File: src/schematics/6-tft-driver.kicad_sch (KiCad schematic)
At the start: 0 parts

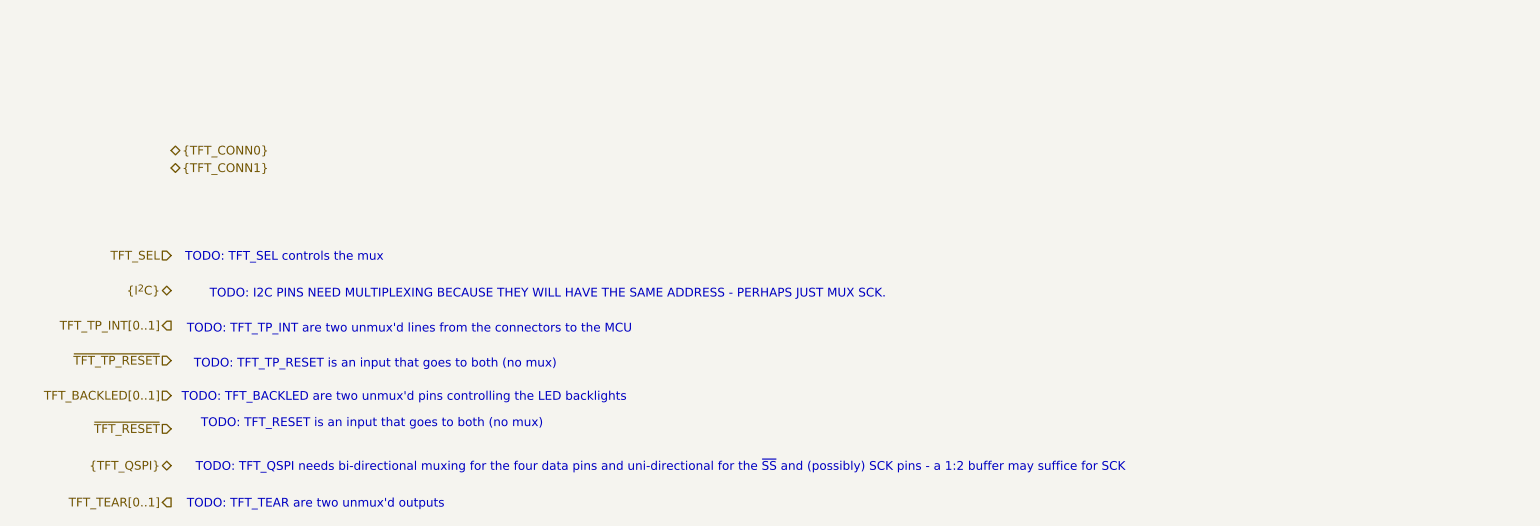
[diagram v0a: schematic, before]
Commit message: Further MCU elaboration and pin mapping.
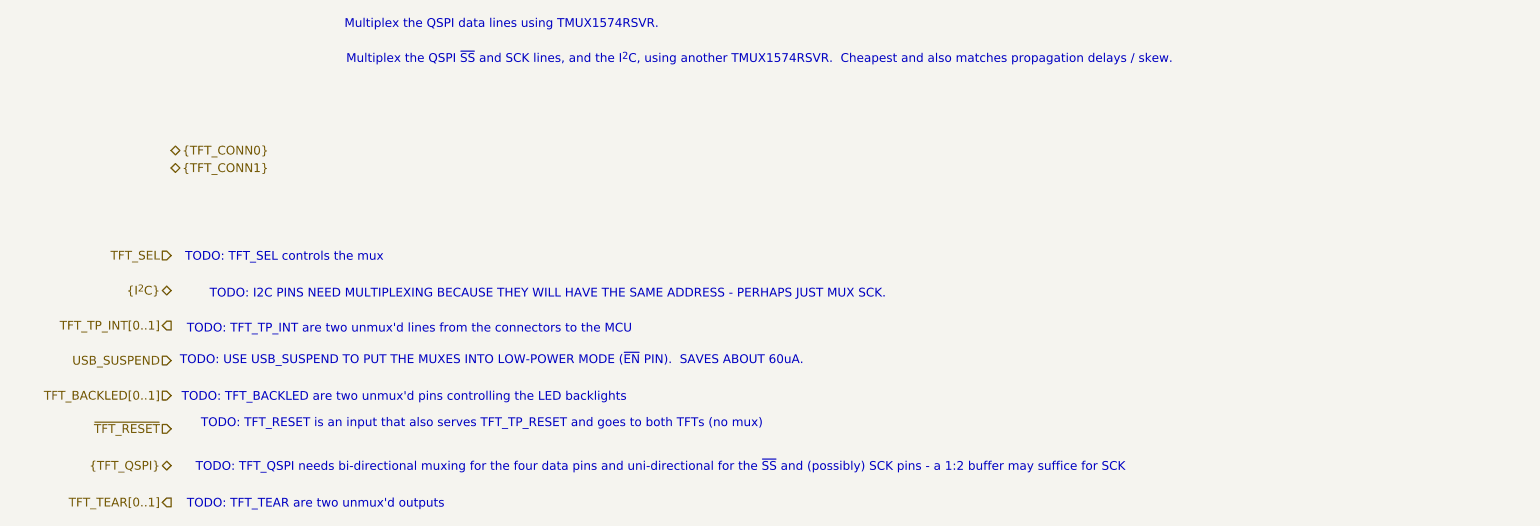
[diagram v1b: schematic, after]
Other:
- note added: "Multiplex the QSPI data lines using TMUX1574RSVR."
- note added: "Multiplex the QSPI ~{SS} and SCK lines, and the I^{2}C, using another TMUX1574RSVR. Cheapest and also matches propagation delays / skew."
- note added: "TODO: TFT_RESET is an input that also serves TFT_TP_RESET and goes to both TFTs (no mux)"
- note added: "TODO: USE USB_SUSPEND TO PUT THE MUXES INTO LOW-POWER MODE (~{EN} PIN). SAVES ABOUT 60uA."
- note removed: "TODO: TFT_RESET is an input that goes to both (no mux)"
- note removed: "TODO: TFT_TP_RESET is an input that goes to both (no mux)"
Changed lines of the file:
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@@
   (bus_alias "TFT_CONN0" (members "TP_SCL" "TP_SDA" "TP_INT" "TP_RST" "LEDA" "LEDK" "L_RES" "L_SDIN" "L_SCLK" "L_IO[1..3]" "L_CS" "L_TE"))
   (bus_alias "TFT_QSPI" (members "~{SS}" "SCK" "DATA[0..3]"))
+  (text "Multiplex the QSPI data lines using TMUX1574RSVR." (at 152.146 119.634 0)
+    (effects (font (size 1.27 1.27)) (justify left bottom))
+  )
   (text "TODO: TFT_QSPI needs bi-directional muxing for the four data pins and uni-directional for the ~{SS} and (possibly) SCK pins - a 1:2 buffer may suffice for SCK"
     (at 130.556 183.896 0)
@@
   (text "TODO: TFT_BACKLED are two unmux'd pins controlling the LED backlights"
     (at 128.524 173.736 0)
-    (effects (font (size 1.27 1.27)) (justify left bottom))
-  )
-  (text "TODO: TFT_TP_RESET is an input that goes to both (no mux)"
-    (at 130.302 168.91 0)
     (effects (font (size 1.27 1.27)) (justify left bottom))
   )
@@
     (effects (font (size 1.27 1.27)) (justify left bottom))
   )
+  (text "TODO: USE USB_SUSPEND TO PUT THE MUXES INTO LOW-POWER MODE (~{EN} PIN).  SAVES ABOUT 60uA."
+    (at 128.27 168.402 0)
+    (effects (font (size 1.27 1.27)) (justify left bottom))
+  )
   (text "TODO: TFT_TP_INT are two unmux'd lines from the connectors to the MCU"
     (at 129.286 163.83 0)
     (effects (font (size 1.27 1.27)) (justify left bottom))
   )
-  (text "TODO: TFT_RESET is an input that goes to both (no mux)"
+  (text "Multiplex the QSPI ~{SS} and SCK lines, and the I^{2}C, using another TMUX1574RSVR.  Cheapest and also matches propagation delays / skew."
+    (at 152.4 124.714 0)
+    (effects (font (size 1.27 1.27)) (justify left bottom))
+  )
+  (text "TODO: TFT_RESET is an input that also serves TFT_TP_RESET and goes to both TFTs (no mux)"
     (at 131.318 177.546 0)
     (effects (font (size 1.27 1.27)) (justify left bottom))
@@
     (effects (font (size 1.27 1.27)) (justify right))
   )
-  (hierarchical_label "~{TFT_TP_RESET}" (shape input) (at 127 167.64 180) (fields_autoplaced)
+  (hierarchical_label "USB_SUSPEND" (shape input) (at 127 167.64 180) (fields_autoplaced)
     (effects (font (size 1.27 1.27)) (justify right))
   )

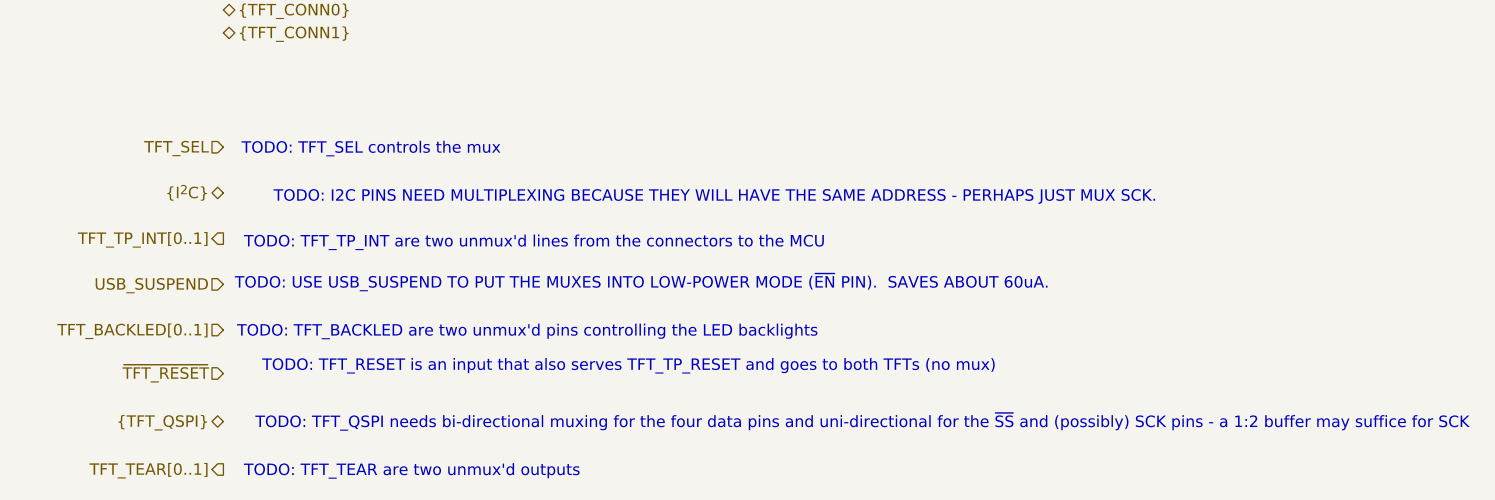
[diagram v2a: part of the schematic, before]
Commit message: Further elaboration of the USB / Power schematic.
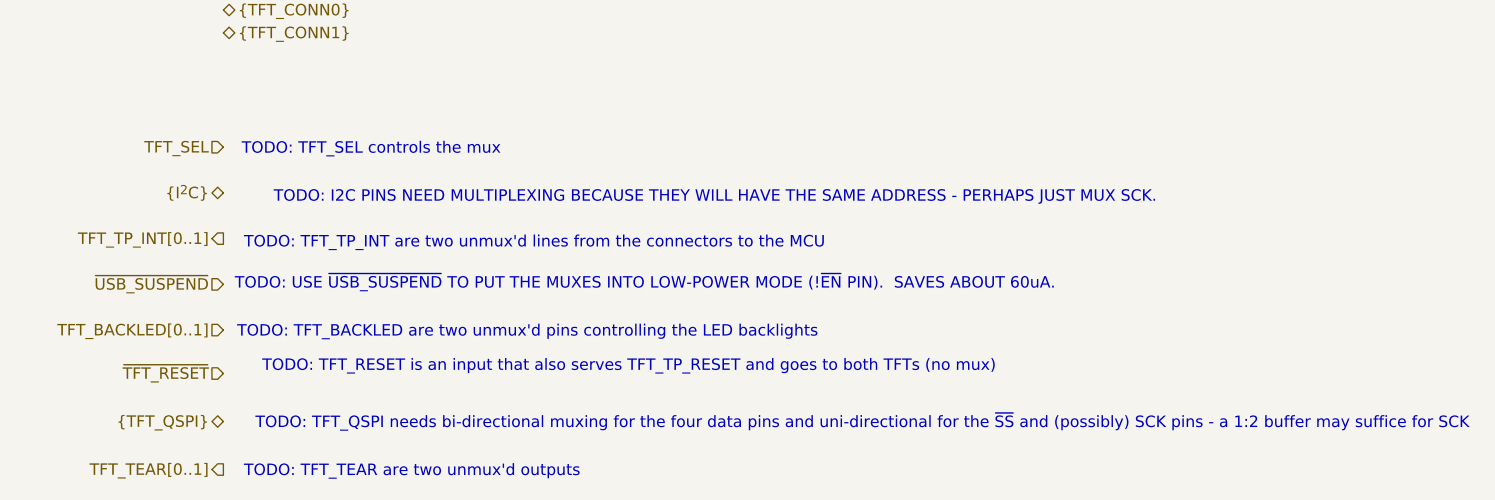
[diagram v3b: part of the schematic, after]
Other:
- note added: "TODO: USE ~{USB_SUSPEND} TO PUT THE MUXES INTO LOW-POWER MODE (!~{EN} PIN). SAVES ABOUT 60uA."
- note removed: "TODO: USE USB_SUSPEND TO PUT THE MUXES INTO LOW-POWER MODE (~{EN} PIN). SAVES ABOUT 60uA."
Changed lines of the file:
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@@
     (effects (font (size 1.27 1.27)) (justify left bottom))
   )
-  (text "TODO: USE USB_SUSPEND TO PUT THE MUXES INTO LOW-POWER MODE (~{EN} PIN).  SAVES ABOUT 60uA."
+  (text "TODO: USE ~{USB_SUSPEND} TO PUT THE MUXES INTO LOW-POWER MODE (!~{EN} PIN).  SAVES ABOUT 60uA."
     (at 128.27 168.402 0)
     (effects (font (size 1.27 1.27)) (justify left bottom))
@@
     (effects (font (size 1.27 1.27)) (justify right))
   )
-  (hierarchical_label "USB_SUSPEND" (shape input) (at 127 167.64 180) (fields_autoplaced)
+  (hierarchical_label "~{USB_SUSPEND}" (shape input) (at 127 167.64 180) (fields_autoplaced)
     (effects (font (size 1.27 1.27)) (justify right))
   )

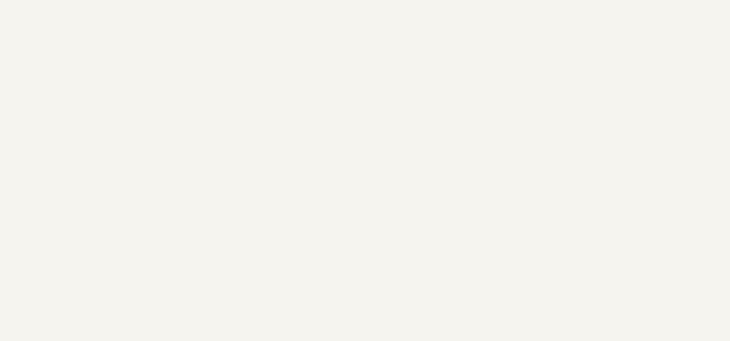
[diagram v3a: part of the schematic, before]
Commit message: Started to draw the MSF receiver based on the simulation learnings.
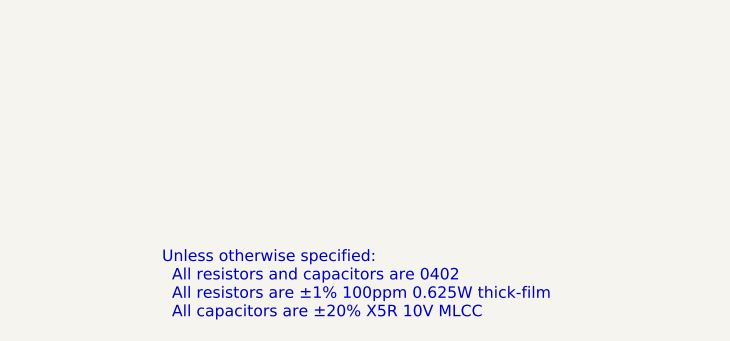
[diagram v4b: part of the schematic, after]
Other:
- note added: "Unless otherwise specified: All resistors and capacitors are 0402 All resistors are ±1% 100ppm 0.625W thick-film All capacitors are ±20% X5R 10V MLCC"
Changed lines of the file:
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@@
+    (effects (font (size 1.27 1.27)) (justify left bottom))
+  )
+  (text "Unless otherwise specified:\n  All resistors and capacitors are 0402\n  All resistors are ±1% 100ppm 0.625W thick-film\n  All capacitors are ±20% X5R 10V MLCC "
+    (at 301.244 261.62 0)
     (effects (font (size 1.27 1.27)) (justify left bottom))
   )

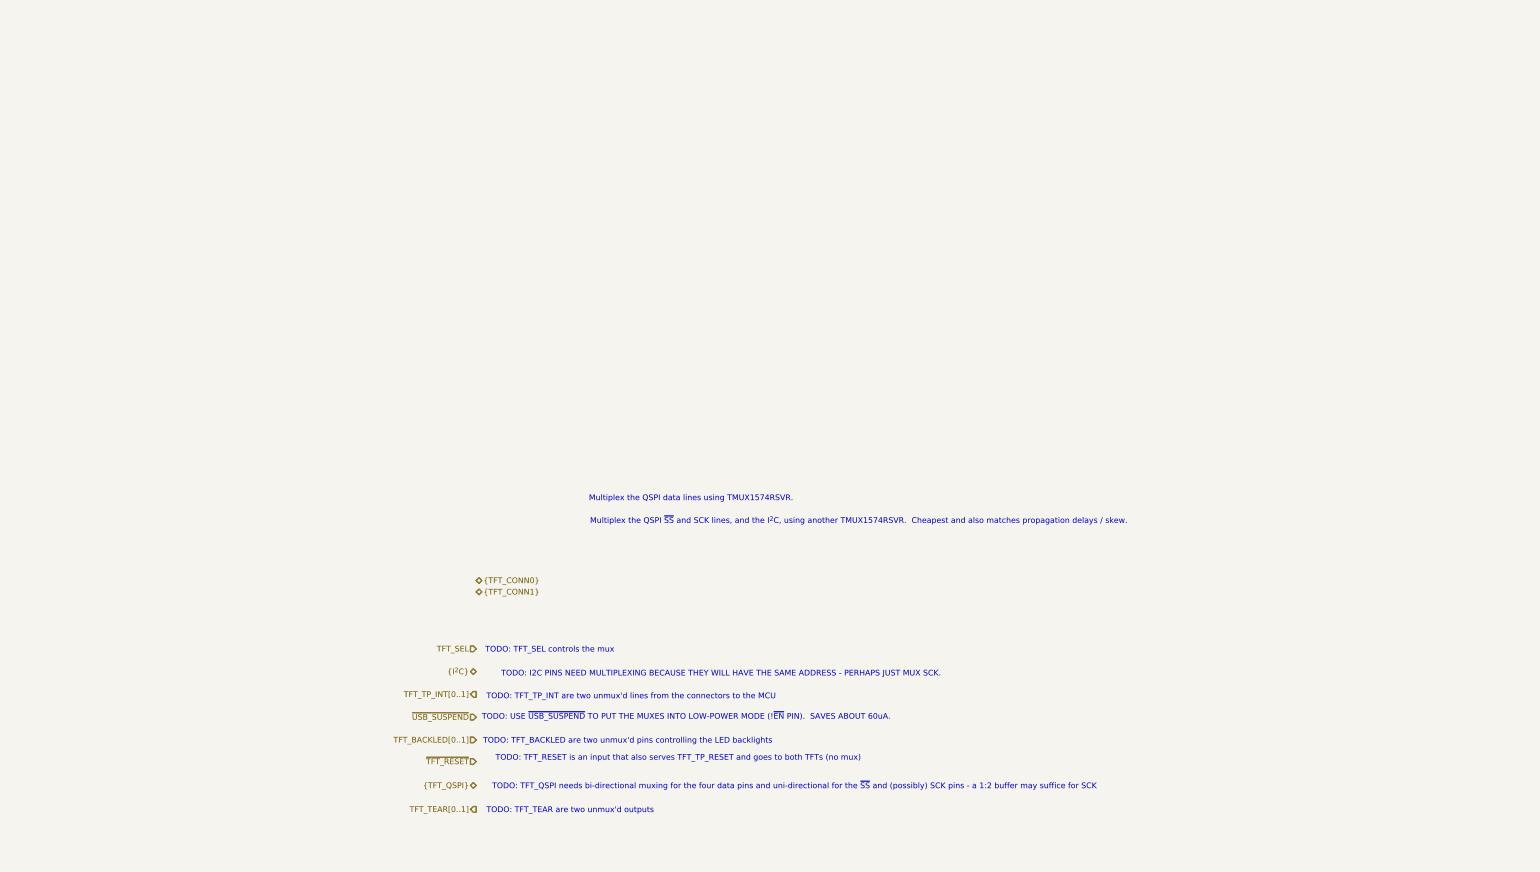
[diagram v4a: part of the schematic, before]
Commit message: Started to draw the TFT module's schematic.
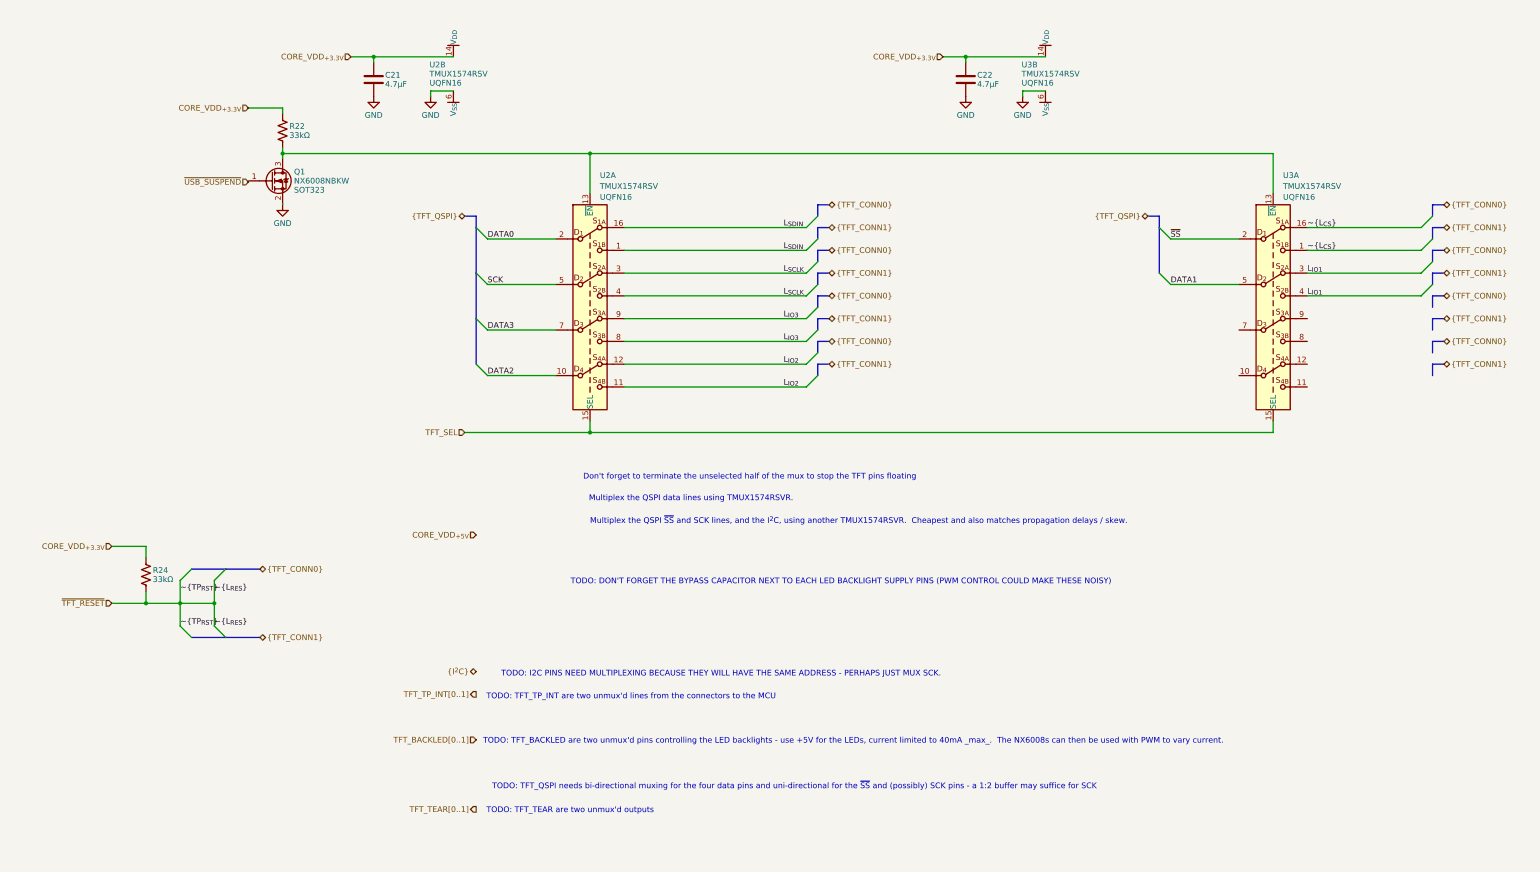
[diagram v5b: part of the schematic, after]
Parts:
- added C21, C22: 4.7μF, restall-generic-capacitors:unpolarised-nominal-0402-1005, symbol restall-generic-capacitors:capacitor-unpolarised
- added Q1: NX6008NBKW, restall-generic-sot:SOT323, symbol restall-manufacturer-nexperia:NX6008NBKW
- added R22, R24: 33kΩ, restall-generic-resistors:nominal-0402-1005, symbol restall-generic-resistors:resistor
- added U2, U3: TMUX1574RSV, restall-manufacturer-ti:UQFN16-1.8x2.6mm-0.4mm, symbol restall-manufacturer-ti:TMUX1574RSV
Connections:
- net TFT_SEL: now also U2.15 (SEL), U3.15 (SEL)
- net ~{TFT_RESET}: now also R24.2
- net ~{USB_SUSPEND}: now also Q1.1 (G)
- new net: Q1.3 (D), R22.2, U2.13 (~{EN}), U3.13 (~{EN})
- new net CORE_VDD_{+3.3V}: C21.1, C22.1, R22.1, R24.1, U2.14 (V_{DD}), U3.14 (V_{DD})
- new net DATA0: U2.2
- new net DATA1: U3.5
- new net DATA2: U2.10
- new net DATA3: U2.7
- new net GND: C21.2, C22.2, Q1.2 (S), U2.6 (V_{SS}), U3.6 (V_{SS})
- new net L_{IO1}: U3.3, U3.4
- new net L_{IO2}: U2.11, U2.12
- new net L_{IO3}: U2.8, U2.9
- new net L_{SCLK}: U2.3, U2.4
- new net L_{SDIN}: U2.1, U2.16
- new net SCK: U2.5
- new net ~{L_{CS}}: U3.1, U3.16
- new net ~{SS}: U3.2
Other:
- note added: "Don't forget to terminate the unselected half of the mux to stop the TFT pins floating"
- note added: "TODO: DON'T FORGET THE BYPASS CAPACITOR NEXT TO EACH LED BACKLIGHT SUPPLY PINS (PWM CONTROL COULD MAKE THESE NOISY)"
- note added: "TODO: TFT_BACKLED are two unmux'd pins controlling the LED backlights - use +5V for the LEDs, current limited to 40mA _max_. The NX6008s can then be used with PWM to vary current."
- note removed: "TODO: TFT_BACKLED are two unmux'd pins controlling the LED backlights"
- note removed: "TODO: TFT_RESET is an input that also serves TFT_TP_RESET and goes to both TFTs (no mux)"
- note removed: "TODO: TFT_SEL controls the mux"
- note removed: "TODO: USE ~{USB_SUSPEND} TO PUT THE MUXES INTO LOW-POWER MODE (!~{EN} PIN). SAVES ABOUT 60uA."

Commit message: Drew the schematic for the TFT driver.
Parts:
- added C603, C604, C605: 4.7μF, restall-generic-capacitors:unpolarised-nominal-0402-1005, symbol restall-generic-capacitors:capacitor-unpolarised
- added Q602, Q603: BC847BS, restall-manufacturer-diodes-inc:SOT363, symbol restall-manufacturer-diodes-inc:BC847BS
- added R602, R603, R604, R605, R606, R607, R608, R609, R610, R611, R612, R613, R615, R616, R617, R618: 33kΩ, restall-generic-resistors:nominal-0402-1005, symbol restall-generic-resistors:resistor
- added R619, R620: 18Ω, restall-generic-resistors:nominal-0402-1005, symbol restall-generic-resistors:resistor
- added U603: TMUX1574RSV, restall-manufacturer-ti:UQFN16-1.8x2.6mm-0.4mm, symbol restall-manufacturer-ti:TMUX1574RSV
- renumbered C21 to C601, C22 to C602, Q1 to Q601, R22 to R601, R24 to R614, U2 to U601, U3 to U602
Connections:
- net CORE_VDD_{+3.3V}: now also C603.1, R610.1, R611.1, R615.1, R616.1, R617.1, R618.1, U603.14 (V_{DD})
- net CORE_VDD_{+5V}: now also C604.1, C605.1
- net GND: now also U602.10, U602.11, U602.12, U602.7, U602.8, U602.9, C603.2, C604.2, C605.2, Q602.1 (E), Q603.1 (E), R602.2, R603.2, R604.2, R605.2, R606.2, R607.2, R608.2, R609.2, R612.2, R613.2, R619.2, R620.2, U603.10, U603.11, U603.12, U603.6 (V_{SS}), U603.7, U603.8, U603.9
- net L_{IO1}: now also R612.1, R613.1
- net L_{IO2}: now also R602.1, R603.1
- net L_{IO3}: now also R604.1, R605.1
- net L_{SCLK}: now also R606.1, R607.1
- net L_{SDIN}: now also R608.1, R609.1
- net ~{L_{CS}}: now also R610.2, R611.2
- net at Q601.3 (D), R601.2, U601.13 (~{EN})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: now also U603.13 (~{EN})
- net TFT_SEL renamed TFT_QSPI_SEL
- new net: Q602.2 (B), Q602.4 (E), R619.1
- new net: Q603.2 (B), Q603.4 (E), R620.1
- new net LED_{K}: Q602.3 (C), Q603.3 (C)
- new net SCL: U603.2
- new net SDA: U603.5
- new net TFT_BACKLED0: Q602.5 (B), Q602.6 (C)
- new net TFT_BACKLED1: Q603.5 (B), Q603.6 (C)
- new net TFT_I^{2}C_SEL: U603.15 (SEL)
- new net TP_SCL: R617.2, R618.2, U603.1, U603.16
- new net TP_SDA: R615.2, R616.2, U603.3, U603.4
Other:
- note added: "Bidirectional QSPI and I^{2}C Multiplexing"
- note added: "Constant-Current LED Backlight Drivers (PWM Brightness Control)"
- note added: "Current sources for roughly 37mA; 31mA-40mA over temperature"
- note added: "R602-R609"
- note added: "R615-R618"
- note added: "Screen and Touch Resets"
- note added: "TODO: SIMULATE (IBIS) THE EFFECTS OF THE PULLS, SERIES R AND MUXES FOR THE QSPI LINES AND THEN ADJUST ACCORDINGLY"
- note added: "Touch and Tear Interrupt Wiring"
- note removed: "Don't forget to terminate the unselected half of the mux to stop the TFT pins floating"
- note removed: "Multiplex the QSPI data lines using TMUX1574RSVR."
- note removed: "Multiplex the QSPI ~{SS} and SCK lines, and the I^{2}C, using another TMUX1574RSVR. Cheapest and also matches propagation delays / skew."
- note removed: "TODO: DON'T FORGET THE BYPASS CAPACITOR NEXT TO EACH LED BACKLIGHT SUPPLY PINS (PWM CONTROL COULD MAKE THESE NOISY)"
- note removed: "TODO: I2C PINS NEED MULTIPLEXING BECAUSE THEY WILL HAVE THE SAME ADDRESS - PERHAPS JUST MUX SCK."
- note removed: "TODO: TFT_BACKLED are two unmux'd pins controlling the LED backlights - use +5V for the LEDs, current limited to 40mA _max_. The NX6008s can then be used with PWM to vary current."
- note removed: "TODO: TFT_QSPI needs bi-directional muxing for the four data pins and uni-directional for the ~{SS} and (possibly) SCK pins - a 1:2 buffer may suffice for SCK"
- note removed: "TODO: TFT_TEAR are two unmux'd outputs"
- note removed: "TODO: TFT_TP_INT are two unmux'd lines from the connectors to the MCU"
- moved on the sheet: C601, C602, Q601, R601, R614, U601A, U601B, U602A, U602B
